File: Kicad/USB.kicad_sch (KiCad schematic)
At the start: 4 parts, among them J1 USB_C_Receptacle_USB2.0

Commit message: power section
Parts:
- J1: footprint Connector_USB:USB_C_Receptacle_Amphenol_12401548E4-2A -> Connector_USB:USB_C_Receptacle_HRO_TYPE-C-31-M-12
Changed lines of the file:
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@@
     (property "Reference" "J1" (id 0) (at 59.69 64.77 0))
     (property "Value" "USB_C_Receptacle_USB2.0" (id 1) (at 59.69 67.31 0))
-    (property "Footprint" "Connector_USB:USB_C_Receptacle_Amphenol_12401548E4-2A" (id 2) (at 63.5 87.63 0)
+    (property "Footprint" "Connector_USB:USB_C_Receptacle_HRO_TYPE-C-31-M-12" (id 2) (at 63.5 87.63 0)
       (effects (font (size 1.27 1.27)) hide)
     )

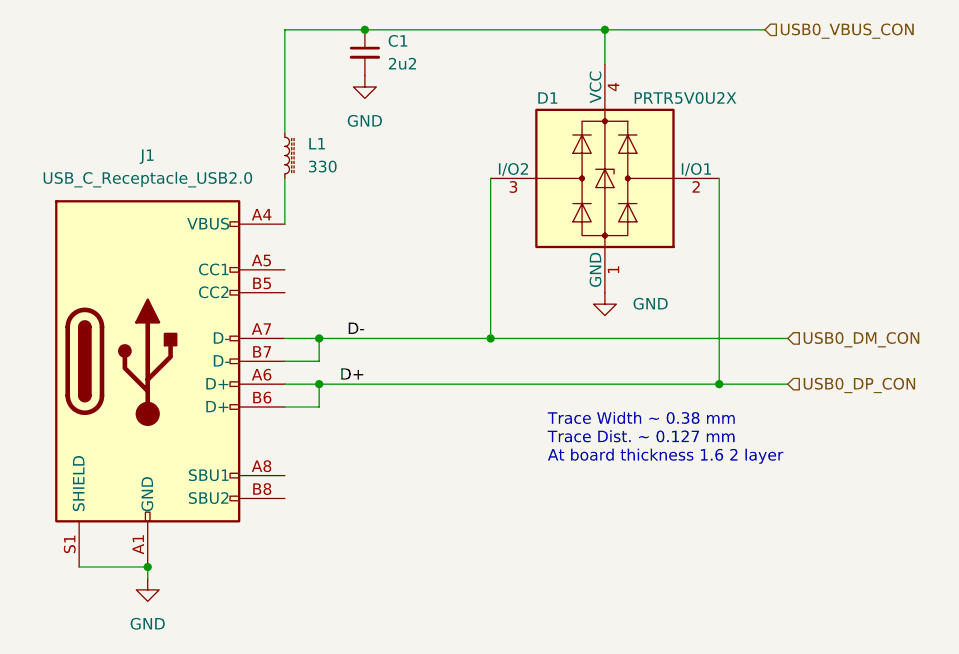
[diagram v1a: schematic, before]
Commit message: updated DAC circut
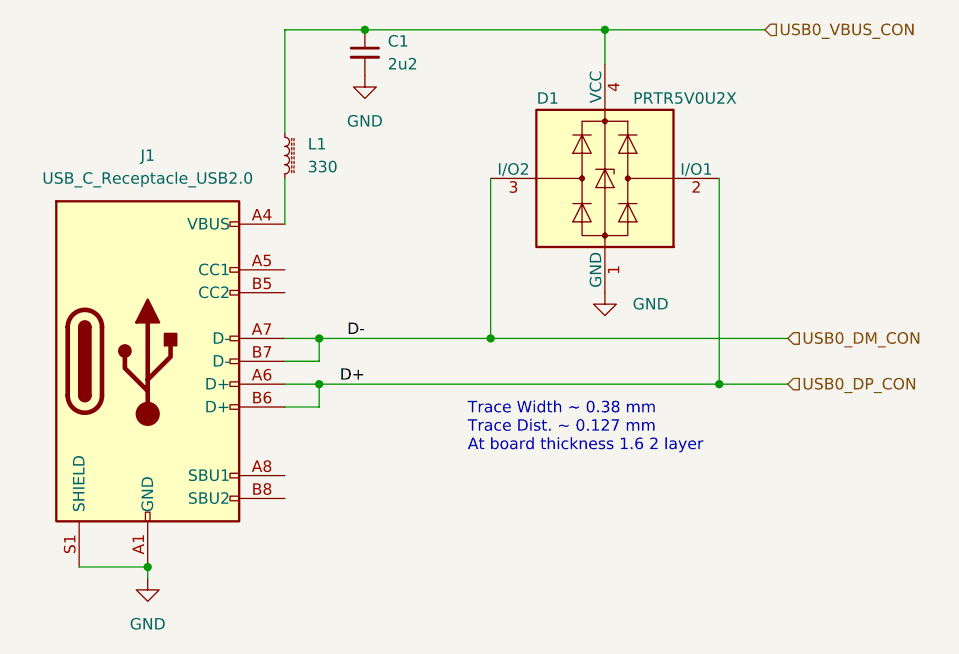
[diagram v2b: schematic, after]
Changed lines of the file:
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@@
   )
   (text "Trace Width ~ 0.38 mm\nTrace Dist. ~ 0.127 mm\nAt board thickness 1.6 2 layer"
-    (at 104.14 99.06 0)
+    (at 95.25 97.79 0)
     (effects (font (size 1.27 1.27)) (justify left bottom))
   )
